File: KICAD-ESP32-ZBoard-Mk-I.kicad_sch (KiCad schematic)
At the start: 25 parts, among them J1 DC_Jack, J2 USB_A, J3 Conn_01x02_Pin-RAIL_1, J4 Conn_01x02_Pin-RAIL_2, J5 Conn_01x02_Pin-RAIL_3, J6 Conn_01x03_Pin-RAIL_1, J7 Conn_01x03_Pin-RAIL_2, J8 Conn_01x03_Pin-RAIL_3, U1 ESP32-WROOM-32UE, U2 SY8120IABC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

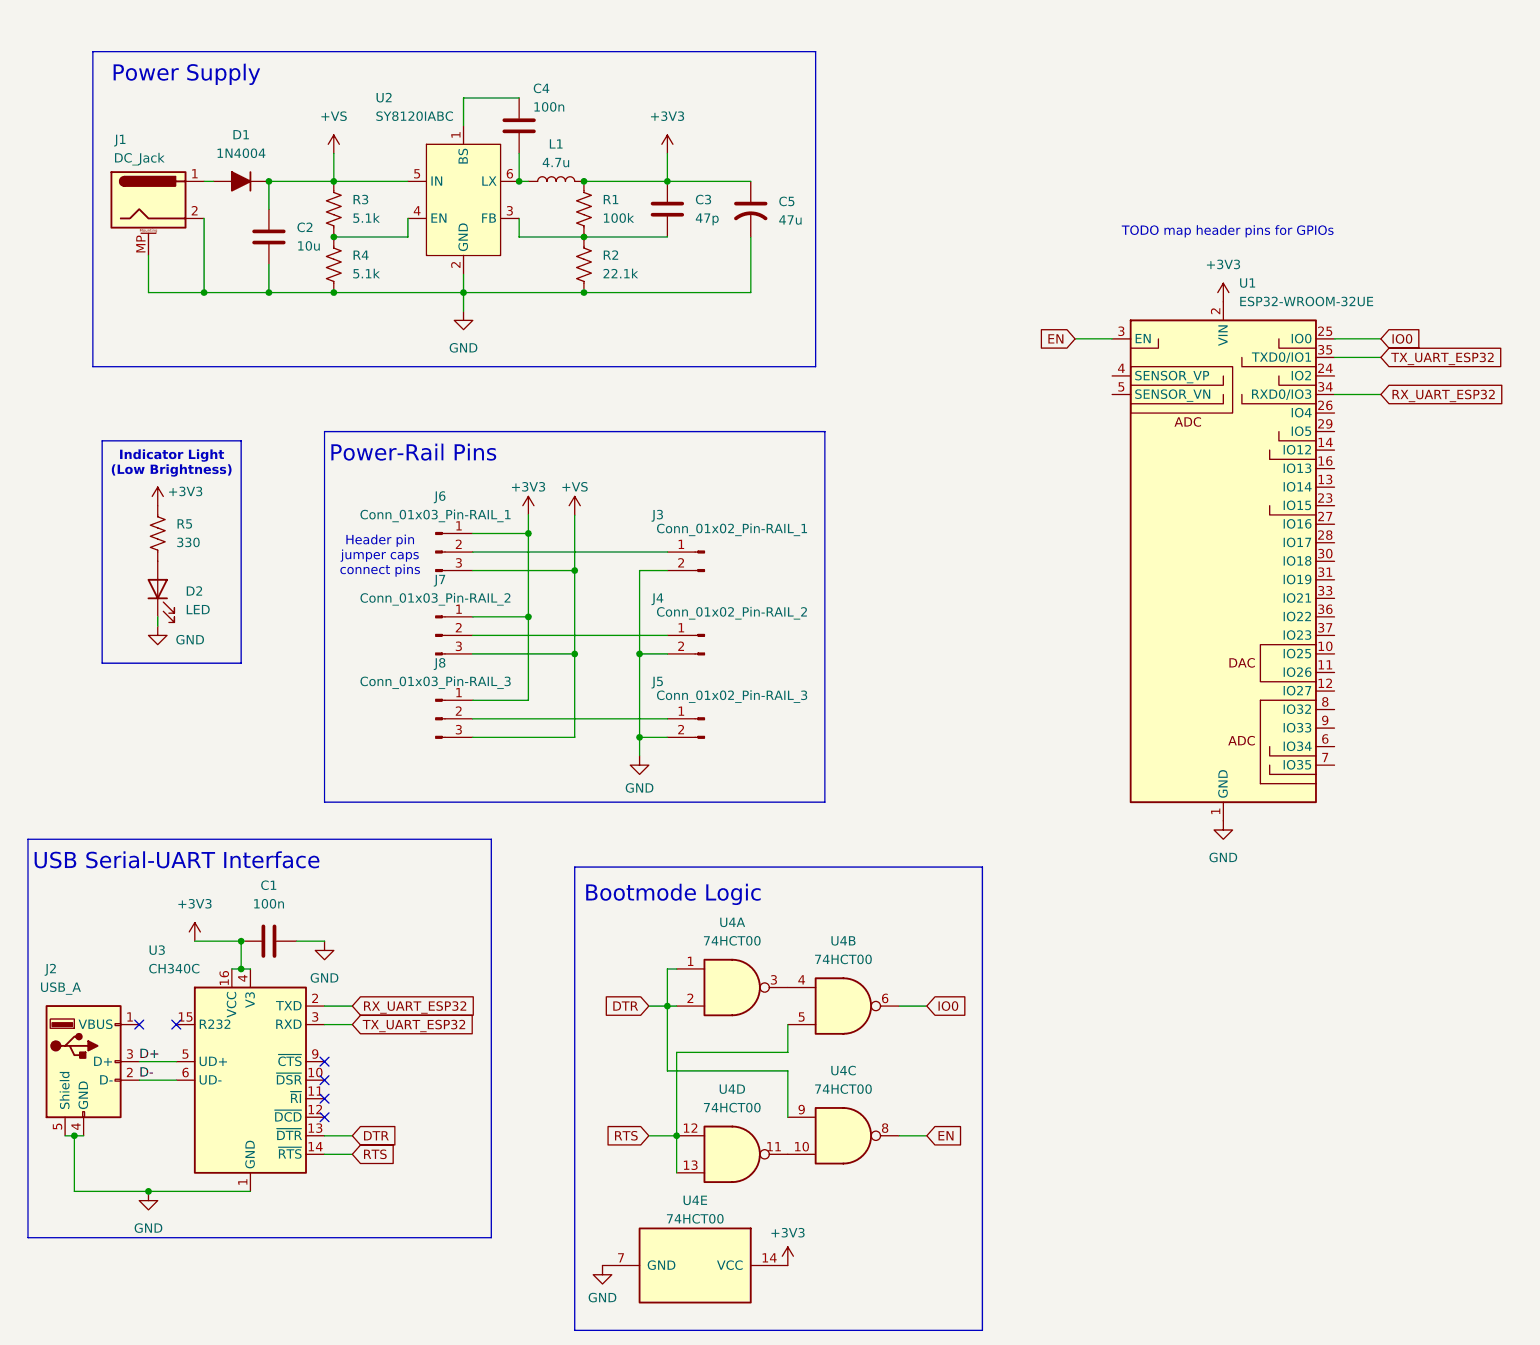
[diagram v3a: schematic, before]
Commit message: ADDED main GPIO header pins, each 01x13.
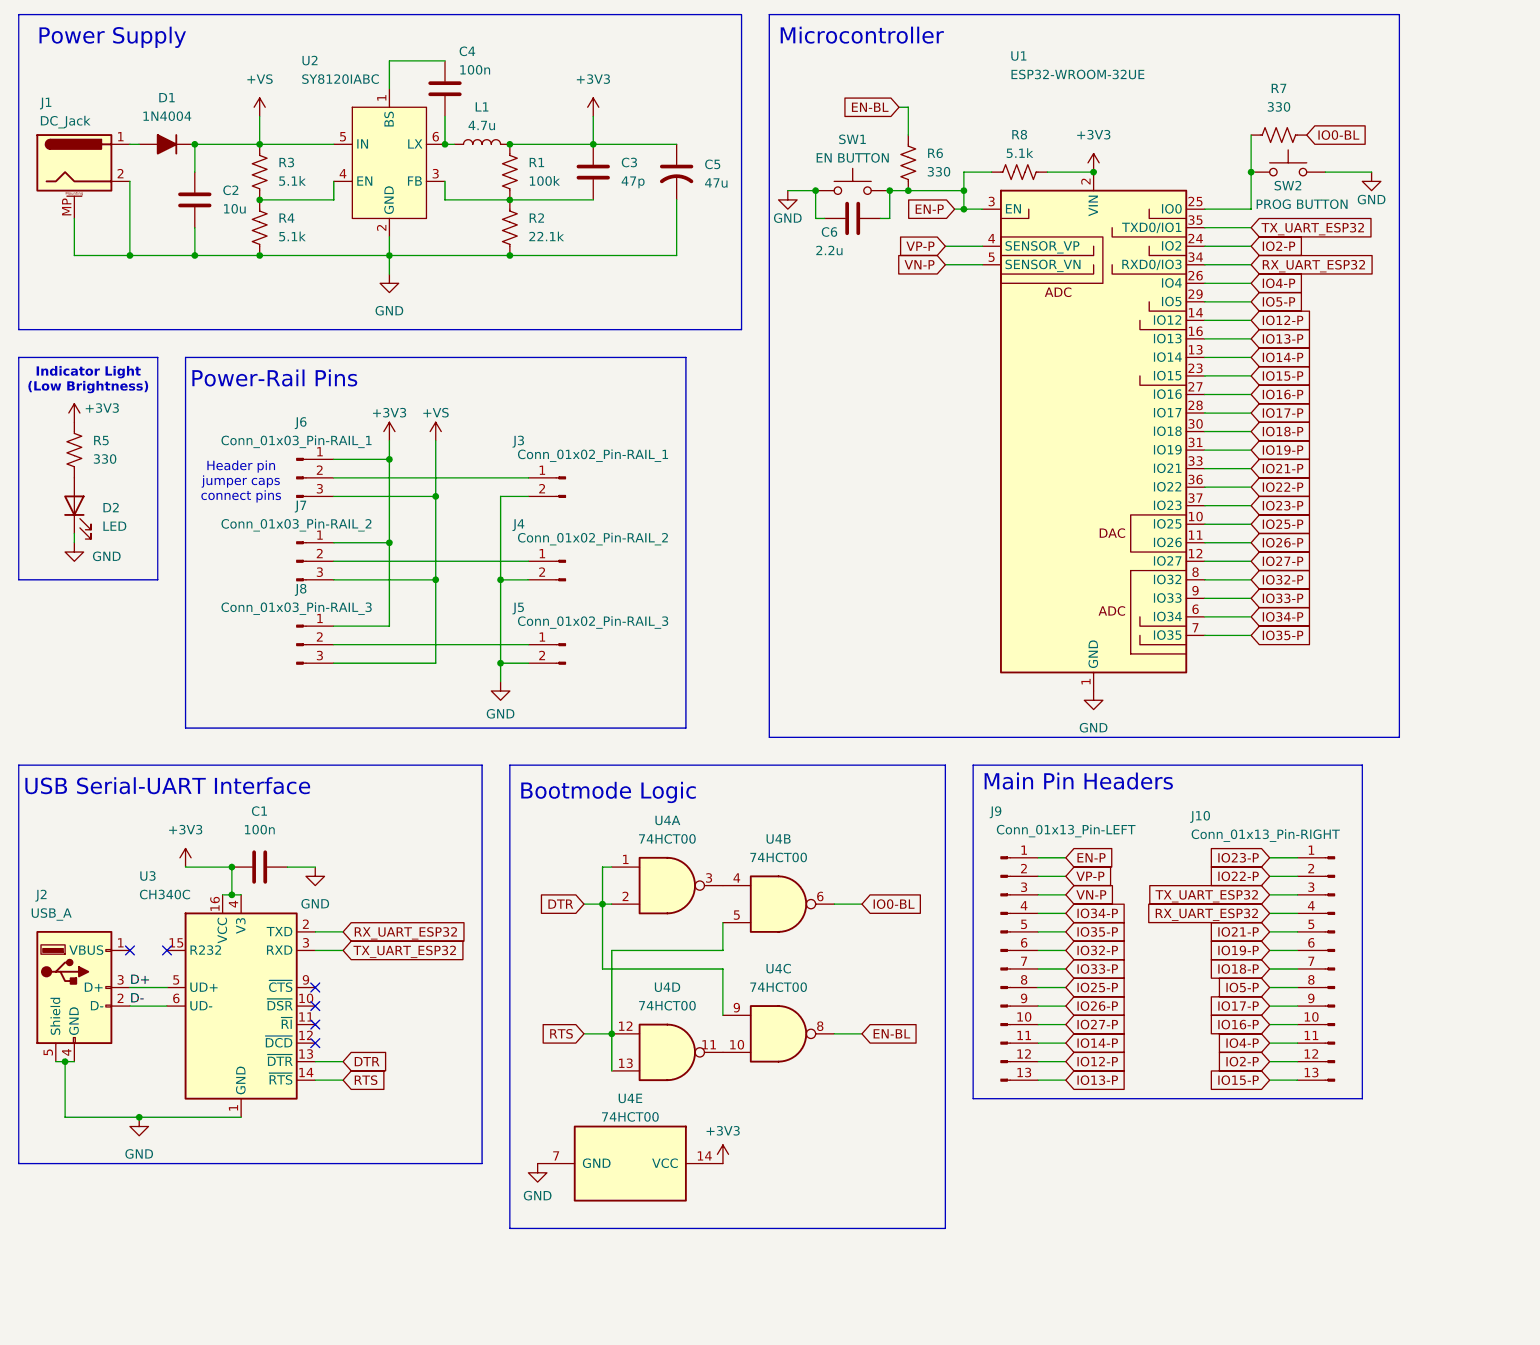
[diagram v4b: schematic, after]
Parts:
- added C6: 2.2u, symbol Device:C
- added J10: Conn_01x13_Pin-RIGHT, Connector_PinHeader_2.54mm:PinHeader_1x13_P2.54mm_Vertical, symbol Connector:Conn_01x13_Pin
- added J9: Conn_01x13_Pin-LEFT, Connector_PinHeader_2.54mm:PinHeader_1x13_P2.54mm_Vertical, symbol Connector:Conn_01x13_Pin
- added R6, R7: 330, symbol Device:R_US
- added R8: 5.1k, symbol Device:R_US
- added SW1: EN BUTTON, symbol Switch:SW_Push
- added SW2: PROG BUTTON, symbol Switch:SW_Push
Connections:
- net +3V3: now also R8.2
- net GND: now also C6.2, SW1.1, SW2.2
- net RX_UART_ESP32: now also J10.4 (Pin_4)
- net TX_UART_ESP32: now also J10.3 (Pin_3)
- net IO25-P: now reaches U1.10 (IO25)
- net IO25-P: now also J9.8 (Pin_8)
- net IO26-P: now reaches U1.11 (IO26)
- net IO26-P: now also J9.9 (Pin_9)
- net IO27-P: now reaches U1.12 (IO27)
- net IO27-P: now also J9.10 (Pin_10)
- net IO14-P: now reaches U1.13 (IO14)
- net IO14-P: now also J9.11 (Pin_11)
- net IO12-P: now reaches U1.14 (IO12)
- net IO12-P: now also J9.12 (Pin_12)
- net IO13-P: now reaches U1.16 (IO13)
- net IO13-P: now also J9.13 (Pin_13)
- net IO15-P: now reaches U1.23 (IO15)
- net IO15-P: now also J10.13 (Pin_13)
- net IO2-P: now reaches U1.24 (IO2)
- net IO2-P: now also J10.12 (Pin_12)
- net IO4-P: now reaches U1.26 (IO4)
- net IO4-P: now also J10.11 (Pin_11)
- net IO16-P: now reaches U1.27 (IO16)
- net IO16-P: now also J10.10 (Pin_10)
- net IO17-P: now reaches U1.28 (IO17)
- net IO17-P: now also J10.9 (Pin_9)
- net IO5-P: now reaches U1.29 (IO5)
- net IO5-P: now also J10.8 (Pin_8)
- net IO18-P: now reaches U1.30 (IO18)
- net IO18-P: now also J10.7 (Pin_7)
- net IO19-P: now reaches U1.31 (IO19)
- net IO19-P: now also J10.6 (Pin_6)
- net IO21-P: now reaches U1.33 (IO21)
- net IO21-P: now also J10.5 (Pin_5)
- net IO22-P: now reaches U1.36 (IO22)
- net IO22-P: now also J10.2 (Pin_2)
- net IO23-P: now reaches U1.37 (IO23)
- net IO23-P: now also J10.1 (Pin_1)
- net VP-P: now reaches U1.4 (SENSOR_VP)
- net VP-P: now also J9.2 (Pin_2)
- net VN-P: now reaches U1.5 (SENSOR_VN)
- net VN-P: now also J9.3 (Pin_3)
- net IO34-P: now reaches U1.6 (IO34)
- net IO34-P: now also J9.4 (Pin_4)
- net IO35-P: now reaches U1.7 (IO35)
- net IO35-P: now also J9.5 (Pin_5)
- net IO32-P: now reaches U1.8 (IO32)
- net IO32-P: now also J9.6 (Pin_6)
- net IO33-P: now reaches U1.9 (IO33)
- net IO33-P: now also J9.7 (Pin_7)
- net EN renamed EN-BL
- net EN-BL: now also R6.1; no longer U1.3 (EN)
- net IO0: no longer names the net of U1.25 (IO0)
- net IO0: now also R7.1, SW2.1; no longer U4.6
- new net EN-P: C6.1, J9.1 (Pin_1), R6.2, R8.1, SW1.2, U1.3 (EN)
- new net IO0-BL: R7.2, U4.6
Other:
- note added: "Main Pin Headers"
- note added: "Microcontroller"
- note removed: "TODO map header pins for GPIOs"
- moved on the sheet: C1, C2, C3, C4, C5, D1, D2, J1, J2, J3, J4, J5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

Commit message: ADDED all LCSC part numbers and footprint assignments.
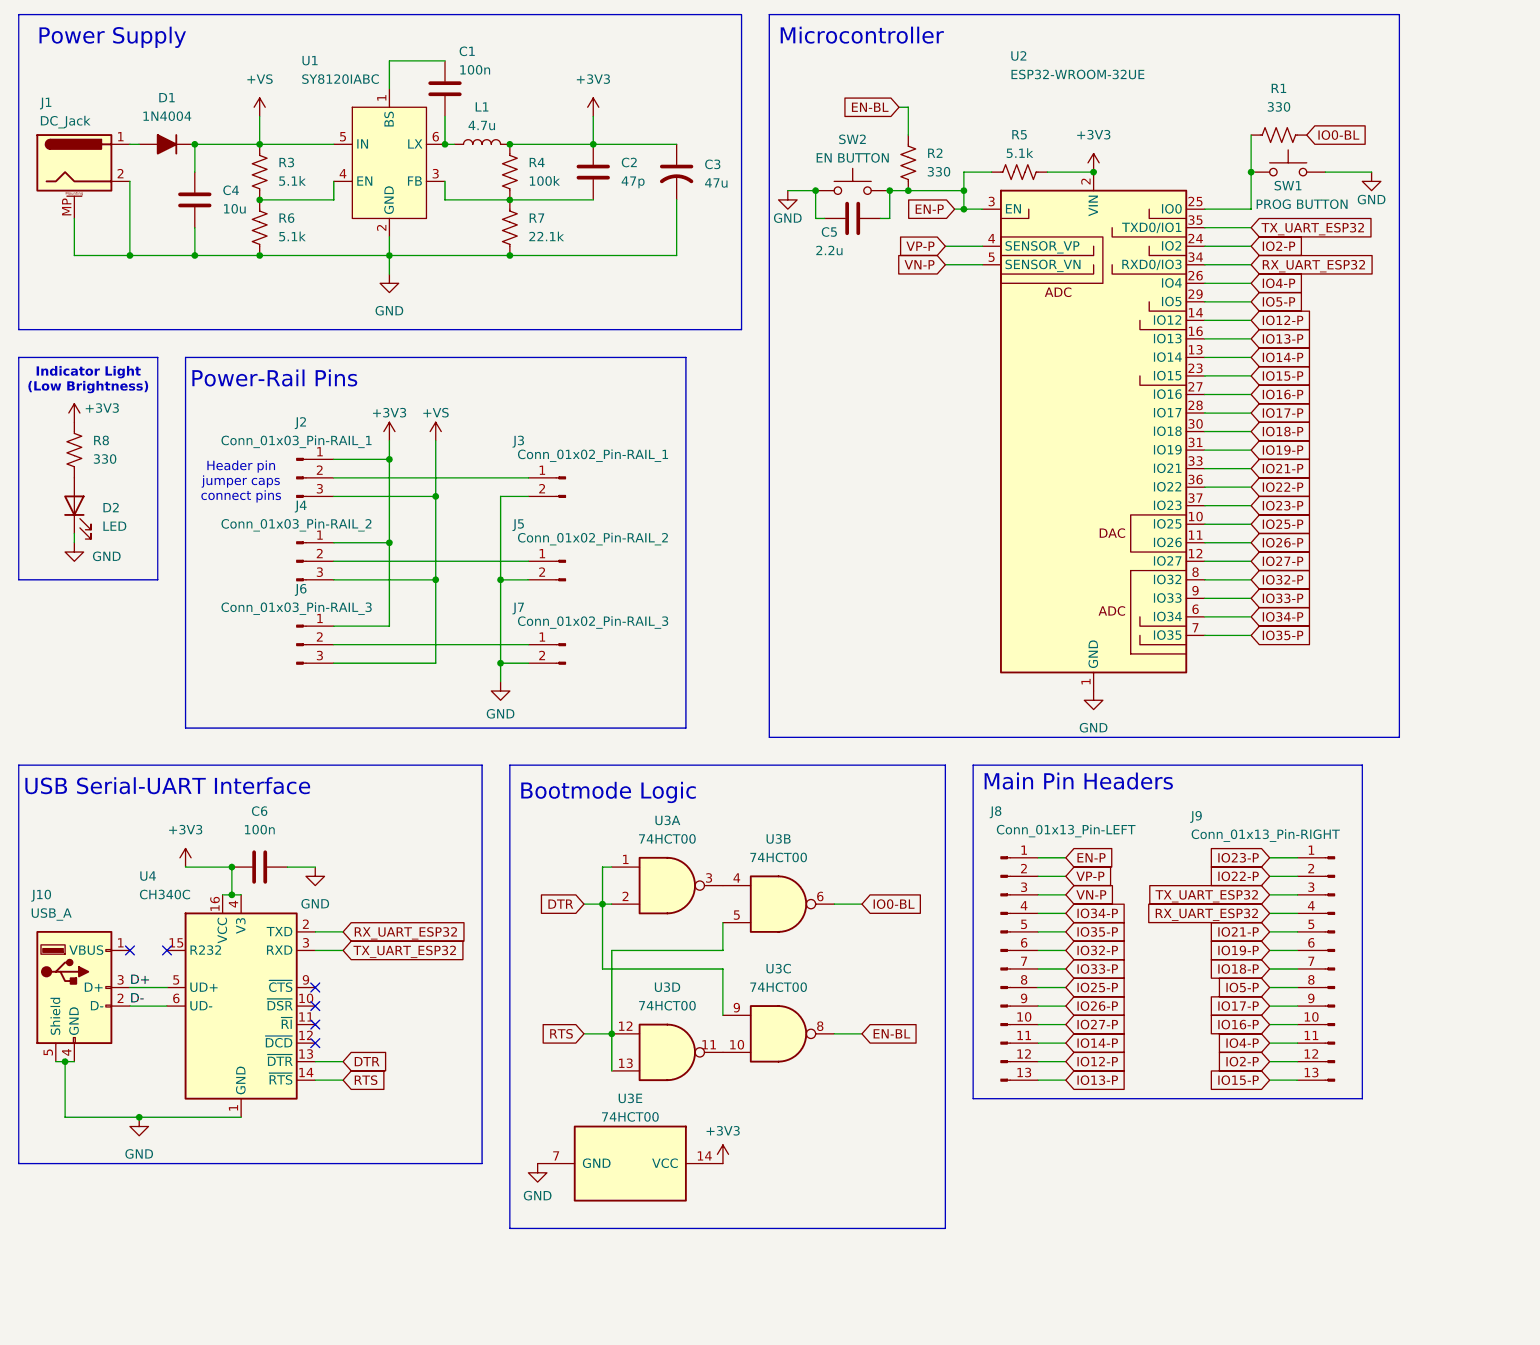
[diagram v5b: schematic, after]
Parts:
- C1: renamed from C4; footprint (none) -> Capacitor_SMD:C_1206_3216Metric_Pad1.33x1.80mm_HandSolder; LCSC Part # (none) -> C97946
- C2: renamed from C3; footprint (none) -> Capacitor_SMD:C_0603_1608Metric_Pad1.08x0.95mm_HandSolder; LCSC Part # (none) -> C882552
- C3: renamed from C5; footprint (none) -> Capacitor_THT:CP_Radial_D5.0mm_P2.50mm; LCSC Part # (none) -> n/a
- C4: renamed from C2; footprint (none) -> Capacitor_SMD:C_0805_2012Metric_Pad1.18x1.45mm_HandSolder; LCSC Part # (none) -> C440198
- C5: renamed from C6; footprint (none) -> Capacitor_SMD:C_0603_1608Metric_Pad1.08x0.95mm_HandSolder; LCSC Part # (none) -> C415535
- C6: renamed from C1; footprint (none) -> Capacitor_SMD:C_1206_3216Metric_Pad1.33x1.80mm_HandSolder; LCSC Part # (none) -> C97946
- D1, J3: LCSC Part # (none) -> n/a
- D2: footprint (none) -> PCM_Diode_SMD_AKL:D_0603_1608Metric_Pad1.05x0.95mm_HandSolder
- J1: LCSC Part # (none) -> C720557
- J10: renamed from J2; footprint (none) -> ZCustomFootprints:USB-A Jing (C42576); LCSC Part # (none) -> C42576
- J2: renamed from J6; LCSC Part # (none) -> n/a
- J4: renamed from J7; LCSC Part # (none) -> n/a
- J5: renamed from J4; LCSC Part # (none) -> n/a
- J6: renamed from J8; LCSC Part # (none) -> n/a
- J7: renamed from J5; LCSC Part # (none) -> n/a
- J8: renamed from J9; LCSC Part # (none) -> n/a
- J9: renamed from J10; LCSC Part # (none) -> n/a
- L1: footprint (none) -> Inductor_SMD:L_TDK_SLF7045; LCSC Part # (none) -> C136201
- R1: renamed from R7; footprint (none) -> PCM_Resistor_SMD_AKL:R_0603_1608Metric; LCSC Part # (none) -> C384242
- R2: renamed from R6; footprint (none) -> PCM_Resistor_SMD_AKL:R_0603_1608Metric; LCSC Part # (none) -> C384242
- R3: footprint (none) -> PCM_Resistor_SMD_AKL:R_0603_1608Metric; LCSC Part # (none) -> C318133
- R4: renamed from R1; footprint (none) -> PCM_Resistor_SMD_AKL:R_0603_1608Metric; LCSC Part # (none) -> C25803
- R5: renamed from R8; footprint (none) -> PCM_Resistor_SMD_AKL:R_0603_1608Metric; LCSC Part # (none) -> C318133
- R6: renamed from R4; footprint (none) -> PCM_Resistor_SMD_AKL:R_0603_1608Metric; LCSC Part # (none) -> C318133
- R7: renamed from R2; footprint (none) -> PCM_Resistor_SMD_AKL:R_0603_1608Metric; LCSC Part # (none) -> C5382621
- R8: renamed from R5; footprint (none) -> PCM_Resistor_SMD_AKL:R_0603_1608Metric; LCSC Part # (none) -> C384242
- SW1: renamed from SW2; footprint (none) -> TS-1101-C-W:SW_101-C-W_XKB; LCSC Part # (none) -> C318938
- SW2: renamed from SW1; footprint (none) -> TS-1101-C-W:SW_101-C-W_XKB; LCSC Part # (none) -> C318938
- U1: renamed from U2; LCSC Part # (none) -> C479076
- U2: renamed from U1; LCSC Part # (none) -> C701344
- U3: renamed from U4; footprint (none) -> Package_DIP:DIP-14_W7.62mm; LCSC Part # (none) -> n/a
- U4: renamed from U3; footprint Package_SO:SOIC-16_3.9x9.9mm_P1.27mm -> Package_SO:SOP-16_3.9x9.9mm_P1.27mm; LCSC Part # (none) -> C84681

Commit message: FINISHED footprint placement. ADDED all routes and planes. TODO finalize silkscreen and adding text and graphics.
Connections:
- net GND: now also J1.3 (MountPin); no longer J1.MP (MountPin)
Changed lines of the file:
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@@
 			)
 		)
-		(pin "MP"
+		(pin "3"
 		)
 		(pin "2"
